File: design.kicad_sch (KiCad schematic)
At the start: 82 parts, among them J1 2601-3108, J10 Conn_01x04, J11 Conn_01x04, J12 Conn_01x03, J13 Conn_01x03, J14 BM04B-SRSS-TB_LF__SN_, J2 2601-3108, J3 2601-3108, J4 TYPE-C-31-M-12, J5 SKEDD-UPDI-4, J6 Conn_01x04, J7 Conn_01x04, J8 Conn_01x04, J9 Conn_01x04, U1 ATtiny1616-S, U2 AP2112K-3.3, U3 CP2105

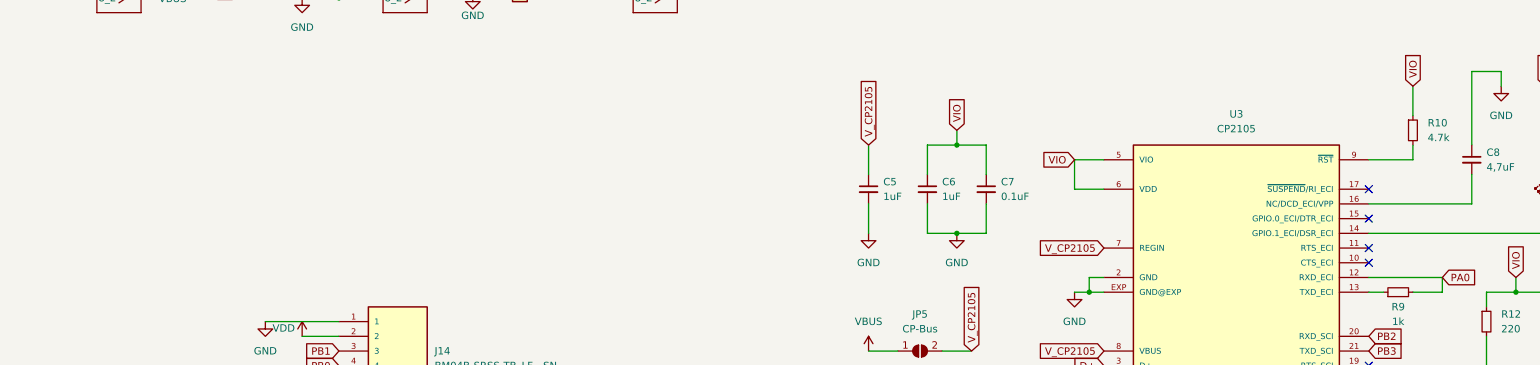
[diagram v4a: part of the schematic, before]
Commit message: Add USB Programming interface
Touchpoints on Back for USB, Power and VPP.
VPP so the 4,7uF capacitor must not be populated and can be done with a programming rig.
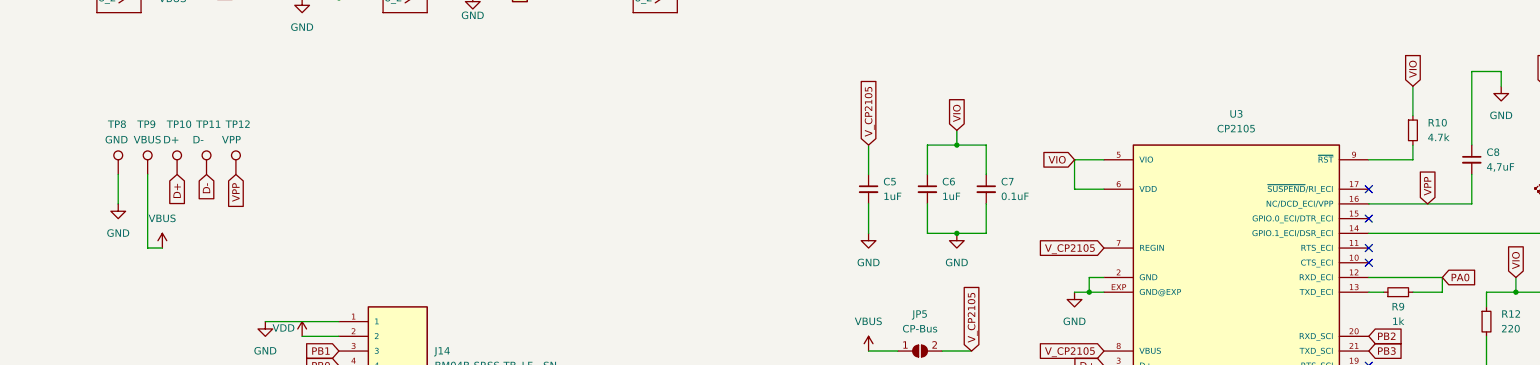
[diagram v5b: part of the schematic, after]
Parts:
- added TP10: D+, TestPoint:TestPoint_Pad_D2.5mm, symbol Connector:TestPoint
- added TP11: D-, TestPoint:TestPoint_Pad_D2.5mm, symbol Connector:TestPoint
- added TP12: VPP, TestPoint:TestPoint_Pad_D2.5mm, symbol Connector:TestPoint
- added TP8: GND, TestPoint:TestPoint_Pad_D2.5mm, symbol Connector:TestPoint
- added TP9: VBUS, TestPoint:TestPoint_Pad_D2.5mm, symbol Connector:TestPoint
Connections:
- net D+: now also TP10.1
- net D-: now also TP11.1
- net GND: now also TP8.1
- net VBUS: now also TP9.1
- net VPP: now reaches C8.2, U3.16 (NC/DCD_ECI/VPP)
- net VPP: now also TP12.1
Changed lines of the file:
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@@
     (stroke (width 0) (type default) (color 0 0 0 0))
   )
+  (wire (pts (xy 38.1 218.44) (xy 38.1 231.14))
+    (stroke (width 0) (type default) (color 0 0 0 0))
+  )
   (wire (pts (xy 259.207 56.642) (xy 263.525 56.642))
     (stroke (width 0) (type default) (color 0 0 0 0))
@@
     (stroke (width 0) (type default) (color 0 0 0 0))
   )
+  (wire (pts (xy 38.1 231.14) (xy 40.64 231.14))
+    (stroke (width 0) (type default) (color 0 0 0 0))
+  )
   (wire (pts (xy 103.378 44.196) (xy 103.378 48.641))
     (stroke (width 0) (type default) (color 0 0 0 0))
@@
     (stroke (width 0) (type default) (color 0 0 0 0))
   )
+  (wire (pts (xy 33.02 218.44) (xy 33.02 223.52))
+    (stroke (width 0) (type default) (color 0 0 0 0))
+  )
   (wire (pts (xy 116.84 154.94) (xy 116.84 157.48))
     (stroke (width 0) (type default) (color 0 0 0 0))
@@
     )
   )
+  (global_label "VPP" (shape input) (at 53.34 218.44 270) (fields_autoplaced)
+    (effects (font (size 1.27 1.27)) (justify right))
+    (property "Referenzen zwischen Schaltplänen" "${INTERSHEET_REFS}" (id 0) (at 53.4194 224.3928 90)
+      (effects (font (size 1.27 1.27)) (justify right) hide)
+    )
+  )
   (global_label "PB4" (shape input) (at 91.44 111.76 0) (fields_autoplaced)
     (effects (font (size 1.27 1.27)) (justify left))
@@
     )
   )
+  (global_label "D+" (shape input) (at 43.18 218.44 270) (fields_autoplaced)
+    (effects (font (size 1.27 1.27)) (justify right))
+    (property "Referenzen zwischen Schaltplänen" "${INTERSHEET_REFS}" (id 0) (at 43.1006 223.6066 90)
+      (effects (font (size 1.27 1.27)) (justify right) hide)
+    )
+  )
   (global_label "D+" (shape input) (at 33.02 35.56 180) (fields_autoplaced)
     (effects (font (size 1.27 1.27)) (justify right))
@@
     )
   )
+  (global_label "VPP" (shape input) (at 259.08 223.52 90) (fields_autoplaced)
+    (effects (font (size 1.27 1.27)) (justify left))
+    (property "Referenzen zwischen Schaltplänen" "${INTERSHEET_REFS}" (id 0) (at 259.0006 217.5672 90)
+      (effects (font (size 1.27 1.27)) (justify left) hide)
+    )
+  )
   (global_label "PB4" (shape input) (at 97.282 179.705 180) (fields_autoplaced)
     (effects (font (size 1.27 1.27)) (justify right))
@@
     )
   )
+  (global_label "D-" (shape input) (at 48.26 218.44 270) (fields_autoplaced)
+    (effects (font (size 1.27 1.27)) (justify right))
+    (property "Referenzen zwischen Schaltplänen" "${INTERSHEET_REFS}" (id 0) (at 48.1806 223.6066 90)
+      (effects (font (size 1.27 1.27)) (justify right) hide)
+    )
+  )
   (global_label "PA6" (shape input) (at 45.339 152.4 180) (fields_autoplaced)
     (effects (font (size 1.27 1.27)) (justify right))
@@
     (pin "2")
   )
+  (symbol (lib_id "power:VBUS") (at 40.64 231.14 0) (unit 1)
+    (in_bom yes) (on_board yes)
+    (property "Reference" "#PWR0192" (id 0) (at 40.64 234.95 0)
+      (effects (font (size 1.27 1.27)) hide)
+    )
+    (property "Value" "VBUS" (id 1) (at 40.64 226.06 0))
+    (property "Footprint" "" (id 2) (at 40.64 231.14 0)
+      (effects (font (size 1.27 1.27)) hide)
+    )
+    (property "Datasheet" "" (id 3) (at 40.64 231.14 0)
+      (effects (font (size 1.27 1.27)) hide)
+    )
+    (pin "1")
+  )
   (symbol (lib_id "Device:C_Small") (at 162.56 220.98 0) (unit 1)
     (in_bom yes) (on_board yes) (fields_autoplaced)
@@
     (pin "4")
   )
+  (symbol (lib_id "Connector:TestPoint") (at 38.1 218.44 0) (unit 1)
+    (in_bom yes) (on_board yes)
+    (property "Reference" "TP9" (id 0) (at 36.322 209.804 0)
+      (effects (font (size 1.27 1.27)) (justify left))
+    )
+    (property "Value" "VBUS" (id 1) (at 35.687 212.471 0)
+      (effects (font (size 1.27 1.27)) (justify left))
+    )
+    (property "Footprint" "TestPoint:TestPoint_Pad_D2.5mm" (id 2) (at 43.18 218.44 0)
+      (effects (font (size 1.27 1.27)) hide)
+    )
+    (property "Datasheet" "~" (id 3) (at 43.18 218.44 0)
+      (effects (font (size 1.27 1.27)) hide)
+    )
+    (pin "1")
+  )
   (symbol (lib_id "Snapeda:CP2105") (at 226.06 241.3 0) (unit 1)
     (in_bom yes) (on_board yes) (fields_autoplaced)
@@
     (pin "1")
   )
+  (symbol (lib_id "Connector:TestPoint") (at 43.18 218.44 0) (unit 1)
+    (in_bom yes) (on_board yes)
+    (property "Reference" "TP10" (id 0) (at 41.402 209.804 0)
+      (effects (font (size 1.27 1.27)) (justify left))
+    )
+    (property "Value" "D+" (id 1) (at 40.767 212.471 0)
+      (effects (font (size 1.27 1.27)) (justify left))
+    )
+    (property "Footprint" "TestPoint:TestPoint_Pad_D2.5mm" (id 2) (at 48.26 218.44 0)
+      (effects (font (size 1.27 1.27)) hide)
+    )
+    (property "Datasheet" "~" (id 3) (at 48.26 218.44 0)
+      (effects (font (size 1.27 1.27)) hide)
+    )
+    (pin "1")
+  )
   (symbol (lib_id "power:GND") (at 388.62 88.9 0) (unit 1)
     (in_bom yes) (on_board yes) (fields_autoplaced)
@@
     (pin "1")
   )
+  (symbol (lib_id "Connector:TestPoint") (at 48.26 218.44 0) (unit 1)
+    (in_bom yes) (on_board yes)
+    (property "Reference" "TP11" (id 0) (at 46.482 209.804 0)
+      (effects (font (size 1.27 1.27)) (justify left))
+    )
+    (property "Value" "D-" (id 1) (at 45.847 212.471 0)
+      (effects (font (size 1.27 1.27)) (justify left))
+    )
+    (property "Footprint" "TestPoint:TestPoint_Pad_D2.5mm" (id 2) (at 53.34 218.44 0)
+      (effects (font (size 1.27 1.27)) hide)
+    )
+    (property "Datasheet" "~" (id 3) (at 53.34 218.44 0)
+      (effects (font (size 1.27 1.27)) hide)
+    )
+    (pin "1")
+  )
+  (symbol (lib_id "Connector:TestPoint") (at 33.02 218.44 0) (unit 1)
+    (in_bom yes) (on_board yes)
+    (property "Reference" "TP8" (id 0) (at 31.242 209.804 0)
+      (effects (font (size 1.27 1.27)) (justify left))
+    )
+    (property "Value" "GND" (id 1) (at 30.734 212.471 0)
+      (effects (font (size 1.27 1.27)) (justify left))
+    )
+    (property "Footprint" "TestPoint:TestPoint_Pad_D2.5mm" (id 2) (at 38.1 218.44 0)
+      (effects (font (size 1.27 1.27)) hide)
+    )
+    (property "Datasheet" "~" (id 3) (at 38.1 218.44 0)
+      (effects (font (size 1.27 1.27)) hide)
+    )
+    (pin "1")
+  )
   (symbol (lib_id "Jumper:SolderJumper_2_Bridged") (at 133.35 81.28 0) (unit 1)
     (in_bom yes) (on_board yes) (fields_autoplaced)
@@
     (pin "1")
   )
+  (symbol (lib_id "power:GND") (at 33.02 223.52 0) (unit 1)
+    (in_bom yes) (on_board yes) (fields_autoplaced)
+    (property "Reference" "#PWR0191" (id 0) (at 33.02 229.87 0)
+      (effects (font (size 1.27 1.27)) hide)
+    )
+    (property "Value" "GND" (id 1) (at 33.02 228.6 0))
+    (property "Footprint" "" (id 2) (at 33.02 223.52 0)
+      (effects (font (size 1.27 1.27)) hide)
+    )
+    (property "Datasheet" "" (id 3) (at 33.02 223.52 0)
+      (effects (font (size 1.27 1.27)) hide)
+    )
+    (pin "1")
+  )
   (symbol (lib_id "Connector_Generic:Conn_01x04") (at 51.435 181.864 0) (unit 1)
     (in_bom yes) (on_board yes) (fields_autoplaced)
@@
     (pin "1")
   )
+  (symbol (lib_id "Connector:TestPoint") (at 53.34 218.44 0) (unit 1)
+    (in_bom yes) (on_board yes)
+    (property "Reference" "TP12" (id 0) (at 51.562 209.804 0)
+      (effects (font (size 1.27 1.27)) (justify left))
+    )
+    (property "Value" "VPP" (id 1) (at 50.927 212.471 0)
+      (effects (font (size 1.27 1.27)) (justify left))
+    )
+    (property "Footprint" "TestPoint:TestPoint_Pad_D2.5mm" (id 2) (at 58.42 218.44 0)
+      (effects (font (size 1.27 1.27)) hide)
+    )
+    (property "Datasheet" "~" (id 3) (at 58.42 218.44 0)
+      (effects (font (size 1.27 1.27)) hide)
+    )
+    (pin "1")
+  )
   (symbol (lib_id "power:VDD") (at 76.2 70.612 0) (mirror y) (unit 1)
     (in_bom yes) (on_board yes)
@@
       (reference "#PWR0190") (unit 1) (value "GND") (footprint "")
     )
+    (path "/ed939f60-5d7e-4678-8a58-efb8efe9096e"
+      (reference "#PWR0191") (unit 1) (value "GND") (footprint "")
+    )
+    (path "/5ba1addd-664d-4d7f-b284-06de651846a6"
+      (reference "#PWR0192") (unit 1) (value "VBUS") (footprint "")
+    )
     (path "/5005112b-a25c-4019-a0f7-bec67dd371e4"
       (reference "C1") (unit 1) (value "1uF") (footprint "Capacitor_SMD:C_0805_2012Metric")
@@
       (reference "TP7") (unit 1) (value "GND") (footprint "Snapeda:RCWCTE_TP420X150")
     )
+    (path "/8e482886-cffb-4f5a-ab3e-b8eb7ec0a64c"
+      (reference "TP8") (unit 1) (value "GND") (footprint "TestPoint:TestPoint_Pad_D2.5mm")
+    )
+    (path "/63f7eb88-7bbc-466e-9759-3e0a23dc27ed"
+      (reference "TP9") (unit 1) (value "VBUS") (footprint "TestPoint:TestPoint_Pad_D2.5mm")
+    )
+    (path "/7f85da6e-2730-4769-acf2-2b7676d749e0"
+      (reference "TP10") (unit 1) (value "D+") (footprint "TestPoint:TestPoint_Pad_D2.5mm")
+    )
+    (path "/8cd1fe38-259d-4bcd-825e-9582d0a2e600"
+      (reference "TP11") (unit 1) (value "D-") (footprint "TestPoint:TestPoint_Pad_D2.5mm")
+    )
+    (path "/f3a7294e-076c-47a1-a4ba-ffb8dd9d5f65"
+      (reference "TP12") (unit 1) (value "VPP") (footprint "TestPoint:TestPoint_Pad_D2.5mm")
+    )
     (path "/f4b21601-8c9d-4968-8673-080d1d6d5811"

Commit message: Add ATtiny QFN
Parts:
- added U4: ATtiny1616-M, Package_DFN_QFN:VQFN-20-1EP_3x3mm_P0.4mm_EP1.7x1.7mm, symbol MCU_Microchip_ATtiny:ATtiny1616-M
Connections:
- net GND: now also U4.21 (GND), U4.3 (GND)
- net PA0: now also U4.19 (~{RESET}/PA0)
- net PA1: now also U4.20 (PA1)
- net PA2: now also U4.1 (PA2)
- net PA3: now also U4.2 (PA3)
- net PA4: now also U4.5 (PA4)
- net PA5: now also U4.6 (PA5)
- net PA6: now also U4.7 (PA6)
- net PA7: now also U4.8 (PA7)
- net PB0: now also U4.14 (PB0)
- net PB1: now also U4.13 (PB1)
- net PB2: now also U4.12 (PB2)
- net PB3: now also U4.11 (PB3)
- net PB4: now also U4.10 (PB4)
- net PB5: now also U4.9 (PB5)
- net PC0: now also U4.15 (PC0)
- net PC1: now also U4.16 (PC1)
- net PC2: now also U4.17 (PC2)
- net PC3: now also U4.18 (PC3)
- net VDD: now also U4.4 (VCC)
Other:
- moved on the sheet: U1

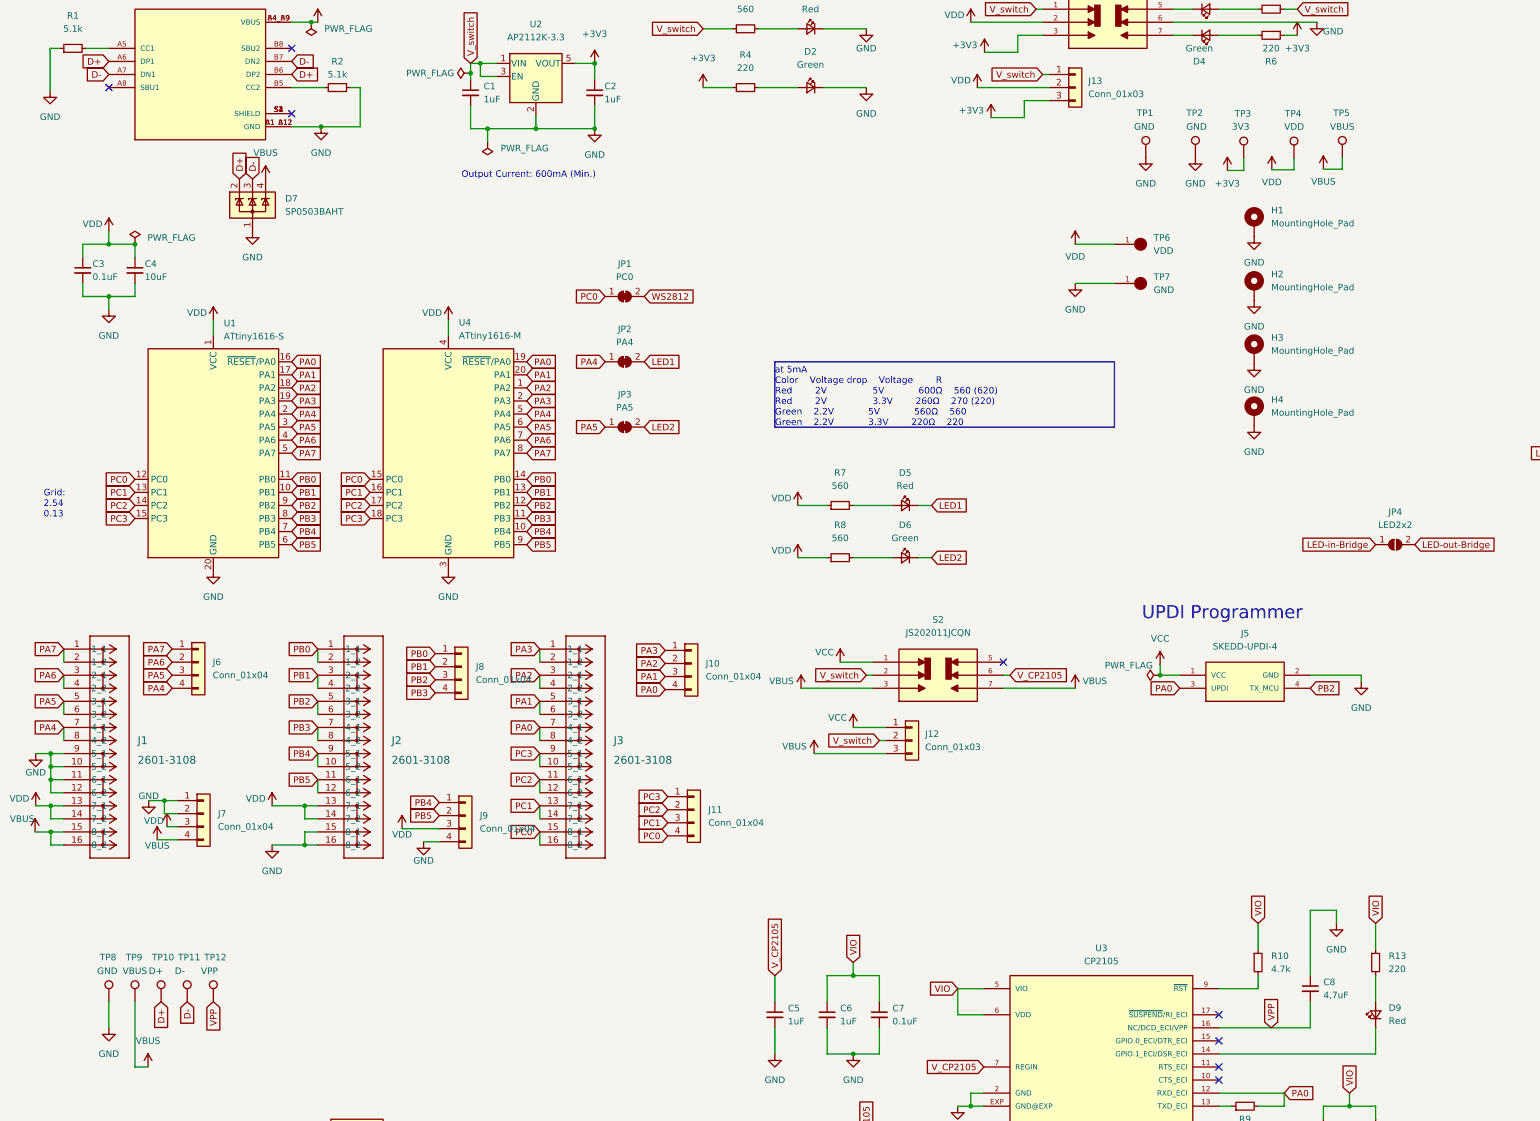
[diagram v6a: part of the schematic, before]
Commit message: add component information
capacitor additional values
JLCPCB part #
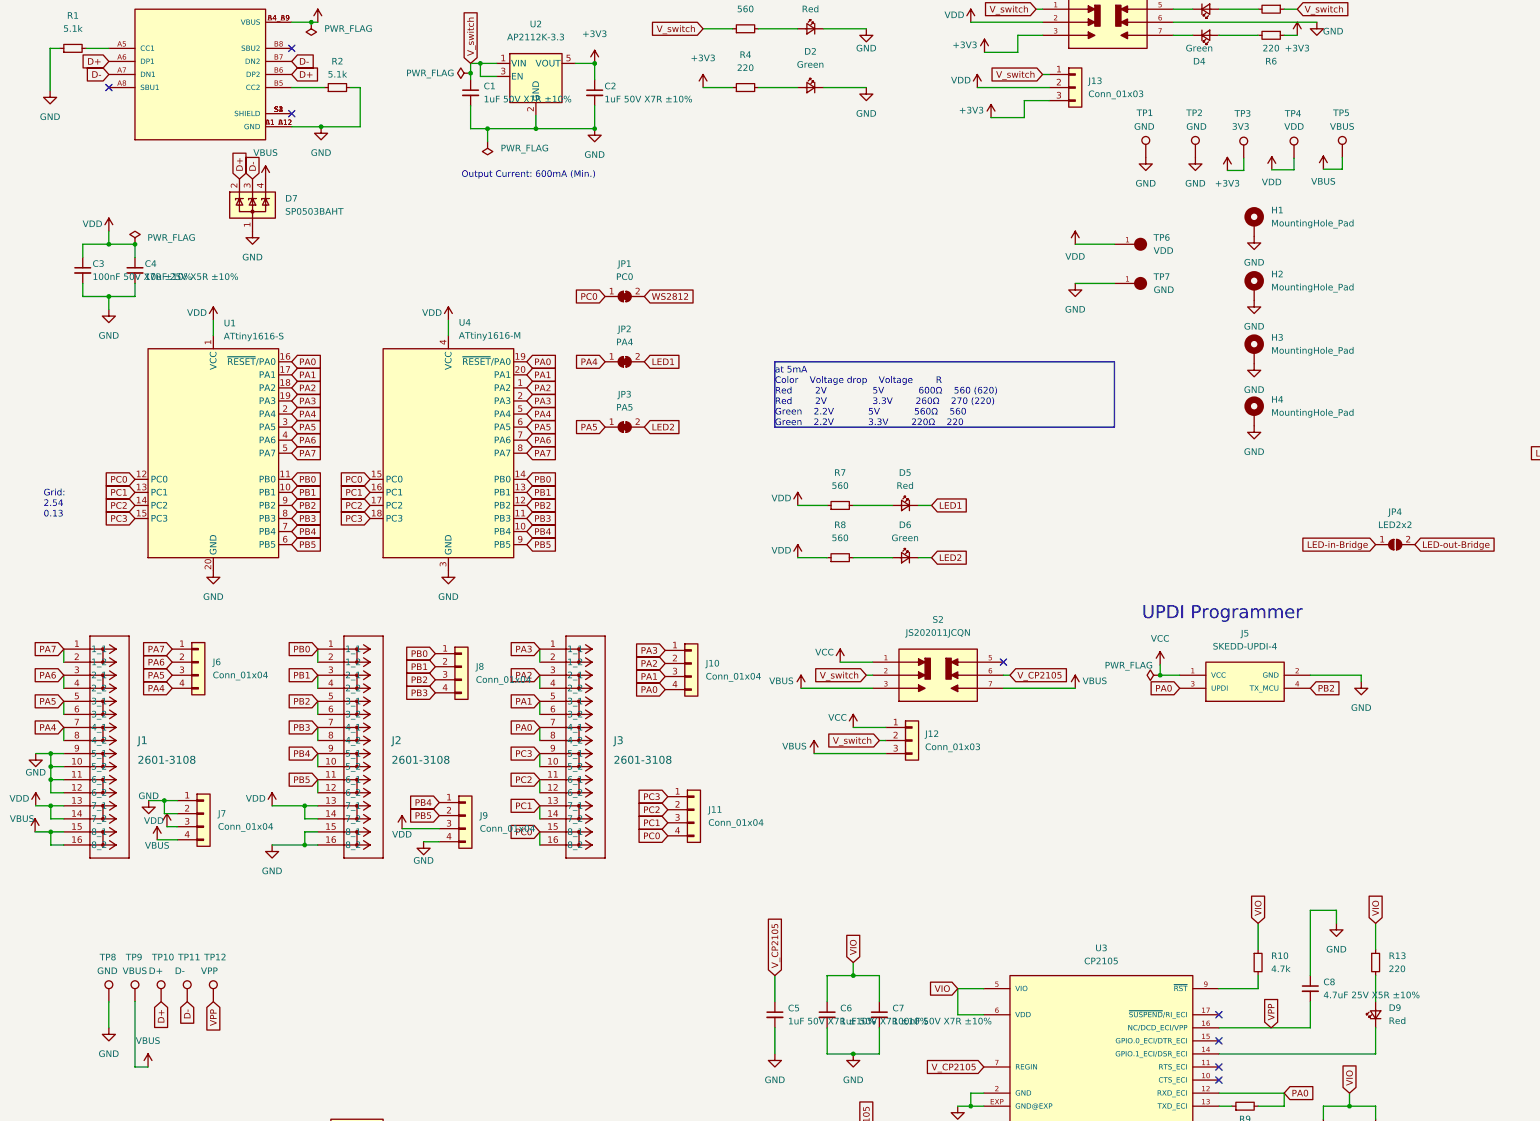
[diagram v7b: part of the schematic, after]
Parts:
- C1, C2, C5, C6: value 1uF -> 1uF 50V X7R ±10%; JLCPCB (none) -> C28323
- C3, C7: value 0.1uF -> 100nF 50V X7R ±10%; JLCPCB (none) -> C49678
- C4: value 10uF -> 10uF 25V X5R ±10%; JLCPCB (none) -> C15850
- C8: value 4,7uF -> 4.7uF 25V X5R ±10%; JLCPCB (none) -> C1779
- D1, D10, D3, D5, D9: JLCPCB (none) -> C84256
- D2, D4, D6, D8: JLCPCB (none) -> C2297
- D7: JLCPCB (none) -> C3040626
- J14: JLCPCB (none) -> C160390
- J4: JLCPCB (none) -> C165948
- LED1, LED10, LED11, LED12, LED13, LED14, LED15, LED16, LED2, LED3, LED4, LED5, LED6, LED7, LED8, LED9: JLCPCB (none) -> C965555
- S1, S2: JLCPCB (none) -> C221665
- U1: JLCPCB (none) -> C614136
- U2: JLCPCB (none) -> C3021085
- U3: JLCPCB (none) -> C109102
- U4: JLCPCB (none) -> C507118
